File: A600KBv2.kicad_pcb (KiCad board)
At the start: 2 copper layers, 316 x 125 mm, 111 parts, among them J1 32 FFC, J2 LED HDR, U1 74LVC2GU04

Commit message: r2
smaller cutouts for stabilizers in PCB
removed unused mounting holes
board shorter by 2mm top/bottom to mount rails
add 0R option to use capslock under keycap only
silkscreen labels for switches
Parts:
- removed the REF** at (352.0, 114.0)
- removed the REF** at (70.0, 136.0)
- removed the REF** at (340.0, 139.0)
- removed the REF** at (122.0, 116.0)
- removed the REF** at (327.0, 50.0)
- removed the REF** at (145.0, 50.0)
- removed the REF** at (278.0, 155.0)
- removed the REF** at (155.0, 99.0)
- removed the REF** at (313.0, 136.0)
- removed the REF** at (255.0, 116.0)
- removed the REF** at (98.0, 97.0)
- removed the REF** at (98.0, 155.0)
- removed the REF** at (250.0, 50.0)
- removed the REF** at (231.0, 98.0)
- removed the REF** at (188.0, 136.0)
- removed the REF** at (69.0, 50.0)
- removed the REF** at (310.0, 98.0)
- removed the REF** at (66.0, 73.0)
- removed the REF** at (340.0, 95.0)
- added R1: 0R, Resistor_SMD:R_0805_2012Metric_Pad1.20x1.40mm_HandSolder, F.Cu at (345.5, 112.0)
- D1: value CAPS LED -> CAPS LED (BLUE)
- D3: value POWER -> POWER LED (RED)
- D4: value FLOPPY -> FLOPPY LED (ORANGE)
- D5: value DISK -> DISK LED (GREEN)
- MX1, MX24: footprint Gateron_KS33_Solderable:Gateron-KS33-Solderable-1.75U -> Amiga Keyboard:Gateron-KS33-Solderable-1.75U
- MX10, MX11, MX14, MX15, MX17, MX20, MX21, MX22, MX23, MX26, MX27, MX28, MX29, MX32, MX33, MX34, MX35, MX38, MX39, MX40, MX41, MX42, MX43, MX47, MX48, MX5, MX50, MX51, MX52, MX53, MX54, MX56, MX57, MX58, MX59, MX6, MX61, MX62, MX63, MX65, MX66, MX67, MX7, MX70, MX72, MX73, MX75, MX76, MX77, MX78, MX8, MX9: footprint Gateron_KS33_Solderable:Gateron-KS33-Solderable-1U -> Amiga Keyboard:Gateron-KS33-Solderable-1U
- MX12, MX13, MX18, MX19, MX2, MX25, MX30, MX31, MX36, MX37, MX46, MX55, MX60, MX64, MX69, MX74: footprint Gateron_KS33_Solderable:Gateron-KS33-Solderable-1.25U -> Amiga Keyboard:Gateron-KS33-Solderable-1.25U
- MX3: footprint Gateron_KS33_Solderable:Gateron-KS33-Solderable-1.5U -> Amiga Keyboard:Gateron-KS33-Solderable-1.5U
- MX4: footprint Amiga_FFC:KS-33-2U-plate-stabilizer -> Amiga Keyboard:Gateron-KS-33-2U-stabilizer
- MX68: footprint Amiga_FFC:KS-33-8_6.25-space-plate-stabilizer -> Amiga Keyboard:KS-33-8U-space
- MX71: footprint Amiga_FFC:KS-33-ISO-plate-stabilizer -> Amiga Keyboard:KS-33-ISO-2U-stabilizer
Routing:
- net Net-(D4-K): track 43.1 -> 58.5 mm
- net Net-(D3-K): track 8.51 -> 17.1 mm, vias 0 -> 2
- net /30: track 483.7 -> 480.3 mm, vias 1 -> 2
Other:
- board size 316 x 125 mm -> 316 x 121 mm
- board text added: "Mechanical keyboard for the A600 - A600KBv2 r2 for Gateron KS-33 low-profile switches aeberbach 07/24 grayunicorn.com LICENSE: CC BY-NC-SA 4.0"
- board text removed: "Mechanical keyboard for the A600 - A600KBv2 r1 for Gateron KS-33 low-profile switches aeberbach 06/24 grayunicorn.com LICENSE: CC BY-NC-SA 4.0"

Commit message: fab 9/7/24 KS-33 revised caps LED
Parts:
- D1: value CAPS LED (BLUE) -> POWER LED (RED)
- D3: value POWER LED (RED) -> CAPS LOCK (BLUE)
- MX71: value RETURN -> CR
- R4: value POWER -> CAPS
- R5: value CAPS -> POWER
- moved R3 4.28 mm to (345.5, 129.0)
- moved R4 2.50 mm to (344.0, 91.5)
- moved R5 2.50 mm to (347.0, 91.5)
- moved R2 1.90 mm to (345.5, 112.5)
- moved R1 1.50 mm to (345.5, 110.5)
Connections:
- D2 pad 2: CAPS_LOCK -> VCC
- J1 pad 9: CAPS_LOCK -> VCC
- U1 pad 1: CAPS_LOCK -> CAPS_GND
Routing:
- net CAPS_LOCK: track 420.5 -> 0.00 mm, vias 6 -> 0
- net CAPS_GND: track 171.6 -> 422.9 mm, vias 3 -> 6
- net VCC: track 0.00 -> 158.8 mm, vias 0 -> 2
- net Net-(D1-K): track 20.7 -> 13.6 mm, vias 2 -> 0
- net Net-(J2-Pin_4): track 17.2 -> 13.0 mm
- net Net-(D5-A): track 3.69 -> 7.97 mm
- net Net-(J2-Pin_3): track 9.97 -> 12.5 mm
- net Net-(J2-Pin_2): track 50.9 -> 53.4 mm
- net Net-(D3-A): track 3.04 -> 5.54 mm
- net Net-(D1-A): track 3.04 -> 5.54 mm
- net Net-(D4-A): track 3.38 -> 5.28 mm
- net Net-(D4-K): track 58.5 -> 60.3 mm
- net Net-(D3-K): track 17.1 -> 15.6 mm
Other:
- board text added: "A"
- board text added: "K"

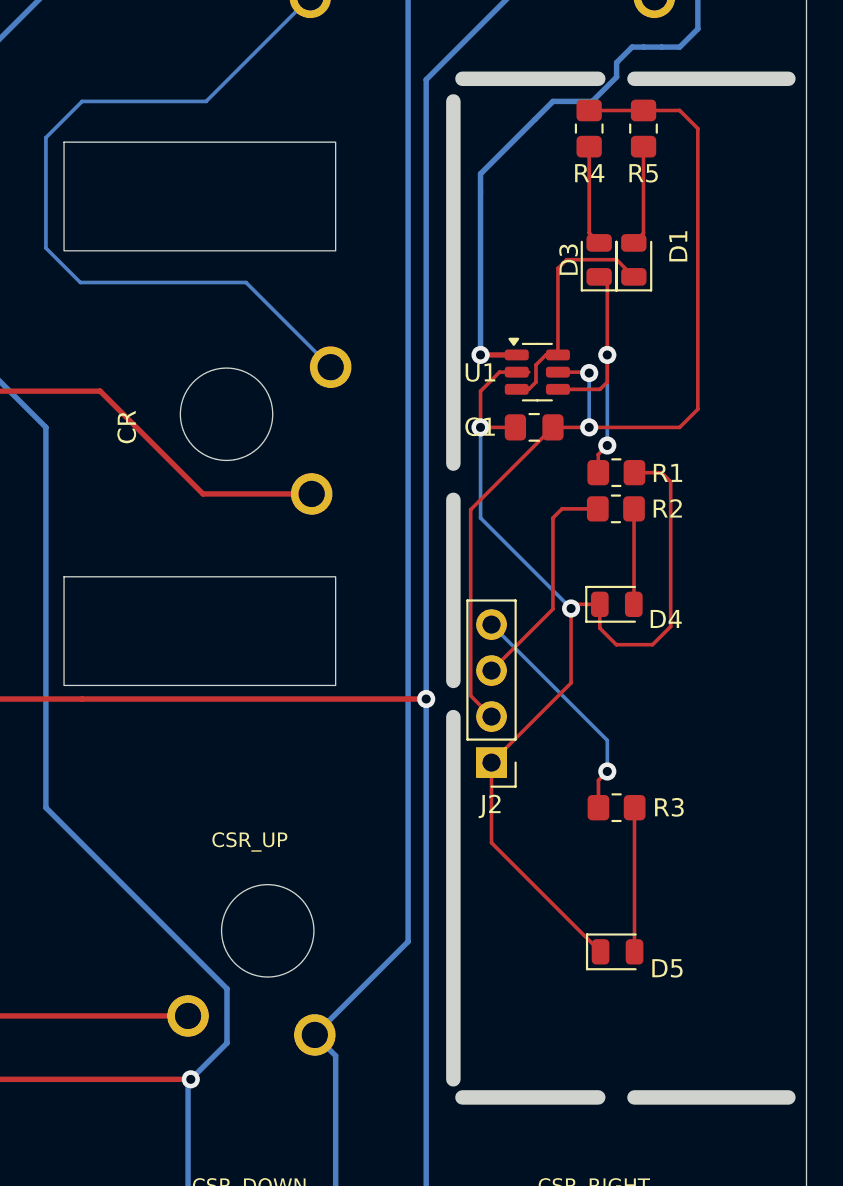
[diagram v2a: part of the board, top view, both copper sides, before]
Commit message: All working with pullups and alt hdd led. New left plate.
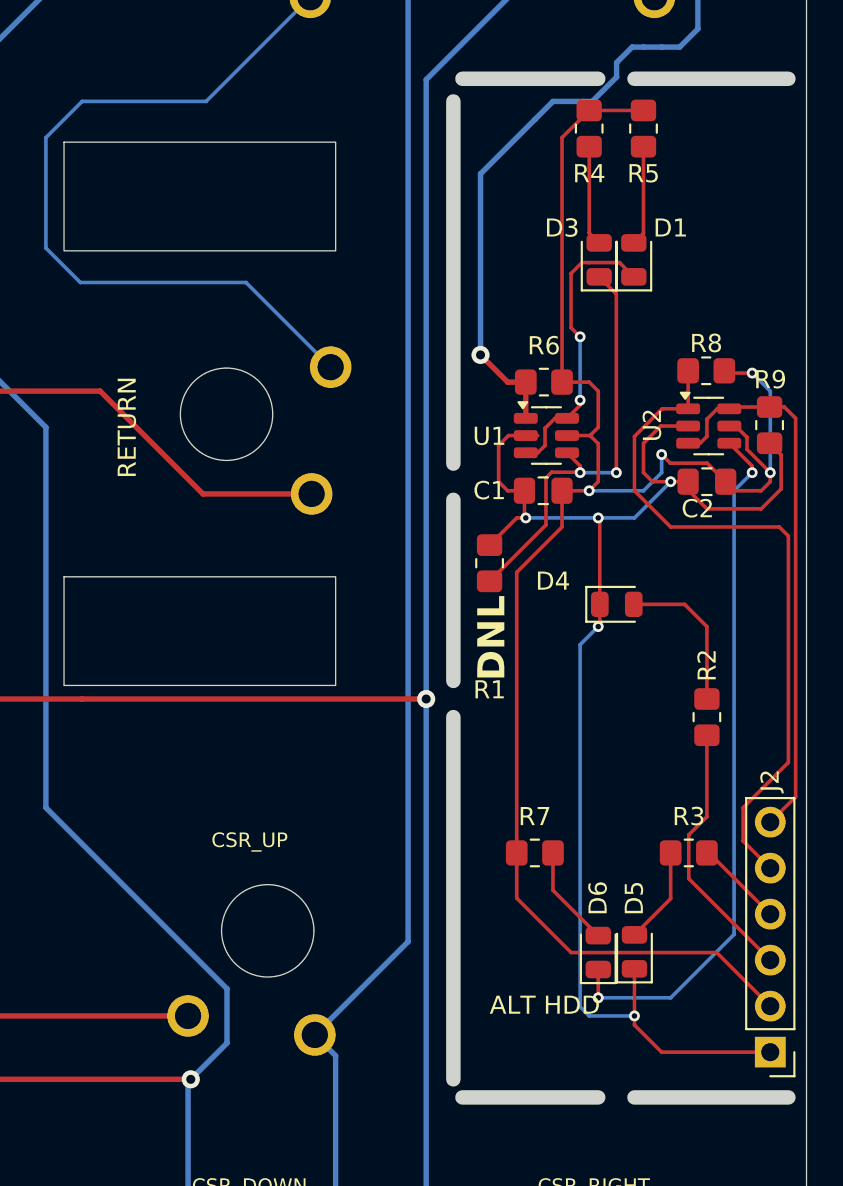
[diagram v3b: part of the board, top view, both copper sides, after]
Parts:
- added C2: .01uF, Capacitor_SMD:C_0805_2012Metric_Pad1.18x1.45mm_HandSolder, F.Cu at (350.5, 111.0)
- added D6: ALT HDD, LED_SMD:LED_0805_2012Metric, F.Cu at (344.5, 137.0)
- added R6: 10k, Resistor_SMD:R_0805_2012Metric_Pad1.20x1.40mm_HandSolder, F.Cu at (341.5, 105.5)
- added R7: ~, Resistor_SMD:R_0805_2012Metric_Pad1.20x1.40mm_HandSolder, F.Cu at (341.0, 131.5)
- added R8: 10k, Resistor_SMD:R_0805_2012Metric_Pad1.20x1.40mm_HandSolder, F.Cu at (350.5, 104.9)
- added R9: 10k, Resistor_SMD:R_0805_2012Metric_Pad1.20x1.40mm_HandSolder, F.Cu at (354.0, 107.9)
- added U2: 74LVC2GU04, Package_TO_SOT_SMD:SOT-23-6, F.Cu at (350.6, 107.9)
- J2: value LED HDR -> Conn_01x06_Pin; footprint Connector_PinHeader_2.54mm:PinHeader_1x04_P2.54mm_Vertical -> Connector_PinHeader_2.54mm:PinHeader_1x06_P2.54mm_Vertical
- MX71: value CR -> RETURN
- moved J2 22.2 mm to (354.0, 142.5)
- moved R2 12.5 mm to (350.5, 124.0), turned to 90 degrees
- moved R1 8.60 mm to (338.5, 115.5), turned to 90 degrees
- moved R3 4.71 mm to (349.5, 131.5), turned to 180 degrees
- moved C1 3.54 mm to (341.5, 111.5)
- moved U1 3.54 mm to (341.6, 108.5)
- moved D5 0.93 mm to (346.5, 137.0), turned to 90 degrees
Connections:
- net Net-(J2-Pin_2) renamed /LED/Input pullup
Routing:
- net /LED/Input pullup: track 53.4 -> 93.9 mm, vias 2 -> 4
- net Net-(D6-K): track 0.00 -> 38.6 mm, vias 0 -> 2
- net /LED//HDD_LIGHT: track 0.00 -> 38.2 mm
- net /LED/HDD LIGHT: track 0.00 -> 30.5 mm
- net Net-(D4-K): track 60.3 -> 77.3 mm, vias 2 -> 5
- net Net-(J2-Pin_4): track 13.0 -> 4.90 mm, vias 1 -> 0
- net Net-(D3-K): track 15.6 -> 23.6 mm
- net Net-(D6-A): track 0.00 -> 5.60 mm
- net Net-(D4-A): track 5.28 -> 8.57 mm
- net CAPS_GND: track 422.9 -> 426.0 mm
- net Net-(D1-K): track 13.6 -> 16.6 mm, vias 0 -> 2
- net Net-(D5-A): track 7.97 -> 5.35 mm
- net Net-(J2-Pin_3): track 12.5 -> 14.7 mm
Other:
- board text added: "/ALT_HDD"
- board text added: "ALT HDD"
- board text added: "ALT_HDD"
- board text added: "CAPS"
- board text added: "DNL"
- board text added: "GND"
- board text added: "HDD"
- board text added: "VCC"
- board text removed: "COM"
- board text removed: "DISK"
- board text removed: "DSK"
- board text removed: "FLP"
- board text removed: "PWR"

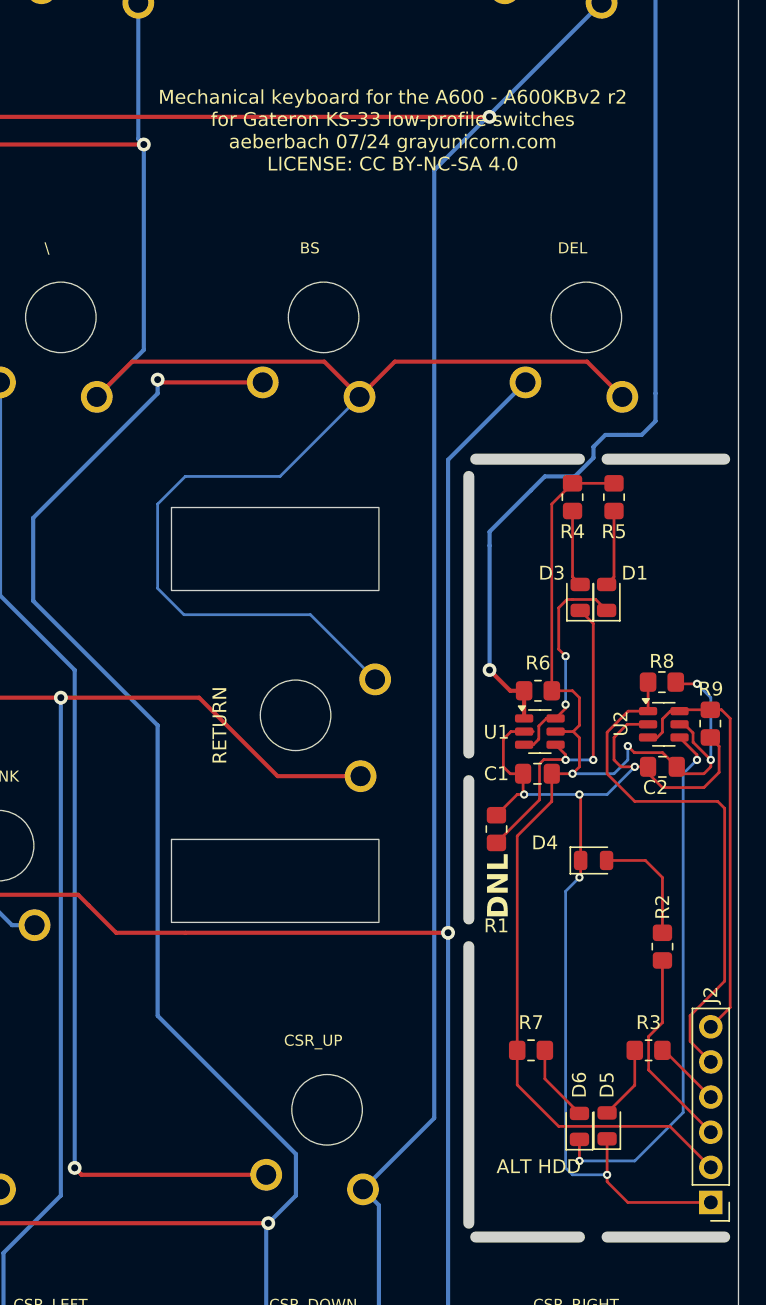
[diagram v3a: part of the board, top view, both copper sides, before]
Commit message: Fix up with pullup resistor for r3
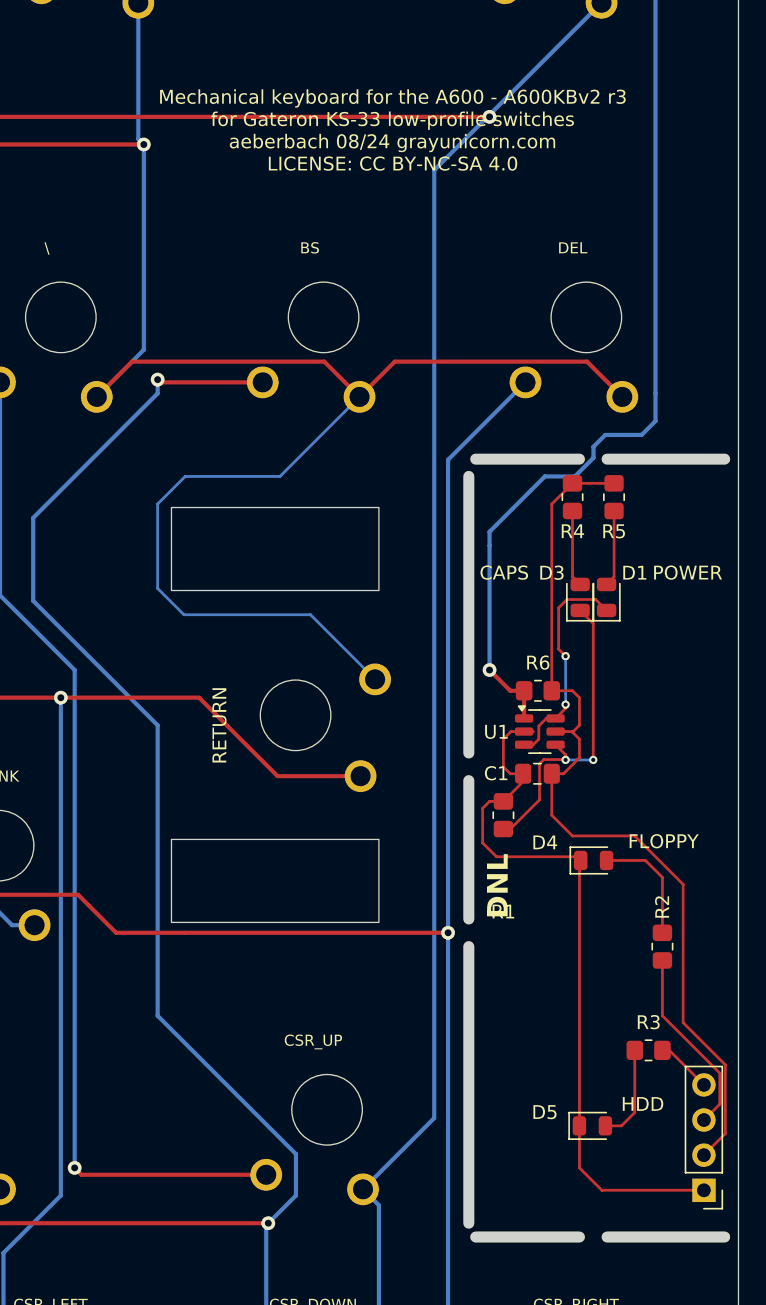
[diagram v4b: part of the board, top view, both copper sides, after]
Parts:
- removed C2: .01uF, Capacitor_SMD:C_0805_2012Metric_Pad1.18x1.45mm_HandSolder
- removed D6: ALT HDD, LED_SMD:LED_0805_2012Metric
- removed R7: ~, Resistor_SMD:R_0805_2012Metric_Pad1.20x1.40mm_HandSolder
- removed R8, R9: 10k, Resistor_SMD:R_0805_2012Metric_Pad1.20x1.40mm_HandSolder
- removed U2: 74LVC2GU04, Package_TO_SOT_SMD:SOT-23-6
- J2: value Conn_01x06_Pin -> Conn_01x04_Pin; footprint Connector_PinHeader_2.54mm:PinHeader_1x06_P2.54mm_Vertical -> Connector_PinHeader_2.54mm:PinHeader_1x04_P2.54mm_Vertical
- moved R1 1.12 mm to (339.0, 114.5)
- moved D5 1.06 mm to (345.4, 137.0), turned to 0 degrees
- moved J2 1.01 mm to (353.5, 141.6)
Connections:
- net /LED/Input pullup renamed Net-(J2-Pin_2)
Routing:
- net Net-(D6-K): track 38.6 -> 0.00 mm, vias 2 -> 0
- net /LED//HDD_LIGHT: track 38.2 -> 0.00 mm
- net /LED/HDD LIGHT: track 30.5 -> 0.00 mm
- net Net-(J2-Pin_2): track 93.9 -> 65.4 mm, vias 4 -> 0
- net Net-(D4-K): track 77.3 -> 52.4 mm, vias 5 -> 0
- net Net-(D6-A): track 5.60 -> 0.00 mm
- net Net-(D5-A): track 5.35 -> 7.02 mm
- net Net-(J2-Pin_3): track 14.7 -> 13.7 mm
- net Net-(D3-K): track 23.6 -> 22.7 mm
- net Net-(J2-Pin_4): track 4.90 -> 4.04 mm
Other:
- board text added: "Mechanical keyboard for the A600 - A600KBv2 r3 for Gateron KS-33 low-profile switches aeberbach 08/24 grayunicorn.com LICENSE: CC BY-NC-SA 4.0"
- board text removed: "/ALT_HDD"
- board text removed: "ALT HDD"
- board text removed: "ALT_HDD"
- board text removed: "GND"
- board text removed: "Mechanical keyboard for the A600 - A600KBv2 r2 for Gateron KS-33 low-profile switches aeberbach 07/24 grayunicorn.com LICENSE: CC BY-NC-SA 4.0"
- board text removed: "VCC"

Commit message: v3
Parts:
- removed REF**: MountingHole_3.2mm_M3, MountingHole:MountingHole_3.2mm_M3
- SPACE: renamed from MX68; footprint Amiga Keyboard:KS-33-8U-space -> Amiga Keyboard:KS-33-8-9U-space
- moved SPACE 0.38 mm to (176.9, 154.9)
- moved MX62 0.15 mm to (278.8, 97.6)
- moved MX66 0.15 mm to (297.8, 97.6)
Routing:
- net /28: track 233.2 -> 233.7 mm
- net CAPS_GND: vias 6 -> 5
